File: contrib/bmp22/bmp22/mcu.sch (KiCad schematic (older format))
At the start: 42 parts, among them J301 USB_C_Receptacle_USB2.0, J302 Conn_ARM_JTAG_SWD_10, SW301 SW_DIP_x01, U301 USBLC6-2SC6, U302 STM32F103CBUx, Y301 8MHz

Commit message: added footprints
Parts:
- C301, C302, C303, C304, C305, C306, C309: footprint (none) -> Capacitor_SMD:C_0402_1005Metric
- C307, C308: footprint (none) -> Capacitor_SMD:C_0603_1608Metric
- D301, D302, D303, D304: footprint (none) -> LED_SMD:LED_0603_1608Metric
- J301: footprint (none) -> Connector_USB:USB_C_Receptacle_Palconn_UTC16-G
- J302: footprint (none) -> Connector:Tag-Connect_TC2050-IDC-NL_2x05_P1.27mm_Vertical
- R301, R302, R303, R304, R305, R308, R309, R310, R311, R312, R313, R314: footprint (none) -> Resistor_SMD:R_0402_1005Metric
- R306, R307: value R -> 5k1; footprint (none) -> Resistor_SMD:R_0402_1005Metric
- SW301: footprint (none) -> Button_Switch_SMD:SW_SPST_PTS810
- TP301, TP302, TP303, TP304, TP305, TP306, TP307, TP308, TP309: footprint (none) -> TestPoint:TestPoint_Pad_1.0x1.0mm

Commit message: created layout
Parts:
- TP301, TP302, TP303, TP304, TP305, TP306, TP307, TP309: footprint TestPoint:TestPoint_Pad_1.0x1.0mm -> TestPoint:TestPoint_Pad_D1.5mm
- TP308: value DIO -> SWDIO; footprint TestPoint:TestPoint_Pad_1.0x1.0mm -> TestPoint:TestPoint_Pad_D1.5mm
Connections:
- net +3V3: now also R311.1; no longer D301.2 (A)
- net GND: now also D301.1 (K), D302.1 (K), D303.1 (K), D304.1 (K); no longer R311.2, R312.2, R313.2, R314.2
- net LED0: now also R312.1; no longer D302.2 (A)
- net LED1: now also R313.1; no longer D303.2 (A)
- net LED2: now also R314.1; no longer D304.2 (A)
- net USBx1+: now also U301.6 (I/O1); no longer U301.4 (I/O2)
- net USBx1-: now also U301.4 (I/O2); no longer U301.6 (I/O1)
- net USBx2+: now also U301.1 (I/O1); no longer U301.3 (I/O2)
- net USBx2-: now also U301.3 (I/O2); no longer U301.1 (I/O1)
- net USB+ renamed USB_P
- net USB- renamed USB_N
- new net: D301.2 (A), R311.2
- new net: D302.2 (A), R312.2
- new net: D303.2 (A), R313.2
- new net: D304.2 (A), R314.2
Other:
- moved on the sheet: D301, D302, D303, D304, R311, R312, R313, R314, TP307, TP308, TP309
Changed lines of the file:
@@
 F 3 "https://www.st.com/resource/en/datasheet/usblc6-2.pdf" H 4150 3950 50  0001 C CNN
 	1    3950 3600
-	1    0    0    -1
+	-1   0    0    -1
 $EndComp
 $Comp
@@
 USBx2-
 Text Label 5550 3700 0    50   ~ 0
-USB-
+USB_N
 Text Label 5550 3500 0    50   ~ 0
-USB+
-Text Label 9300 5150 0    50   ~ 0
-USB+
-Text Label 9300 5050 0    50   ~ 0
-USB-
+USB_P
 Text Label 10150 4750 0    50   ~ 0
-USB+
+USB_P
 $Comp
 L Device:R R309
@@
 F 0 "TP301" H 7600 3150 50  0000 C CNN
 F 1 "~RST" H 7600 3050 50  0000 C CNN
-F 2 "TestPoint:TestPoint_Pad_1.0x1.0mm" H 7800 2850 50  0001 C CNN
+F 2 "TestPoint:TestPoint_Pad_D1.5mm" H 7800 2850 50  0001 C CNN
 F 3 "~" H 7800 2850 50  0001 C CNN
 	1    7600 2850
@@
 L Device:LED D301
 U 1 1 5F2F0E27
+P 1550 6700
+F 0 "D301" H 1550 6800 50  0000 C CNN
+F 1 "GREEN" H 1650 6600 50  0000 C CNN
+F 2 "LED_SMD:LED_0603_1608Metric" H 1550 6700 50  0001 C CNN
+F 3 "~" H 1550 6700 50  0001 C CNN
+	1    1550 6700
+	0    -1   -1   0
+$EndComp
+$Comp
+L Device:R R311
+U 1 1 5F2F3ADD
 P 1550 6400
-F 0 "D301" H 1550 6500 50  0000 C CNN
-F 1 "GREEN" H 1650 6300 50  0000 C CNN
-F 2 "LED_SMD:LED_0603_1608Metric" H 1550 6400 50  0001 C CNN
+F 0 "R311" V 1630 6400 50  0000 C CNN
+F 1 "330" V 1550 6400 50  0000 C CNN
+F 2 "Resistor_SMD:R_0402_1005Metric" V 1480 6400 50  0001 C CNN
 F 3 "~" H 1550 6400 50  0001 C CNN
 	1    1550 6400
-	0    -1   -1   0
-$EndComp
-$Comp
-L Device:R R311
-U 1 1 5F2F3ADD
-P 1550 6700
-F 0 "R311" V 1630 6700 50  0000 C CNN
-F 1 "330" V 1550 6700 50  0000 C CNN
-F 2 "Resistor_SMD:R_0402_1005Metric" V 1480 6700 50  0001 C CNN
-F 3 "~" H 1550 6700 50  0001 C CNN
-	1    1550 6700
 	1    0    0    -1
 $EndComp
@@
 L Device:LED D302
 U 1 1 5F2F57A5
+P 1850 6700
+F 0 "D302" H 1850 6800 50  0000 C CNN
+F 1 "RED" H 1900 6600 50  0000 C CNN
+F 2 "LED_SMD:LED_0603_1608Metric" H 1850 6700 50  0001 C CNN
+F 3 "~" H 1850 6700 50  0001 C CNN
+	1    1850 6700
+	0    -1   -1   0
+$EndComp
+$Comp
+L Device:R R312
+U 1 1 5F2F57AB
 P 1850 6400
-F 0 "D302" H 1850 6500 50  0000 C CNN
-F 1 "RED" H 1900 6300 50  0000 C CNN
-F 2 "LED_SMD:LED_0603_1608Metric" H 1850 6400 50  0001 C CNN
+F 0 "R312" V 1930 6400 50  0000 C CNN
+F 1 "330" V 1850 6400 50  0000 C CNN
+F 2 "Resistor_SMD:R_0402_1005Metric" V 1780 6400 50  0001 C CNN
 F 3 "~" H 1850 6400 50  0001 C CNN
 	1    1850 6400
-	0    -1   -1   0
-$EndComp
-$Comp
-L Device:R R312
-U 1 1 5F2F57AB
-P 1850 6700
-F 0 "R312" V 1930 6700 50  0000 C CNN
-F 1 "330" V 1850 6700 50  0000 C CNN
-F 2 "Resistor_SMD:R_0402_1005Metric" V 1780 6700 50  0001 C CNN
-F 3 "~" H 1850 6700 50  0001 C CNN
-	1    1850 6700
 	1    0    0    -1
 $EndComp
@@
 L Device:LED D303
 U 1 1 5F2F8AB8
+P 2150 6700
+F 0 "D303" H 2150 6800 50  0000 C CNN
+F 1 "ORANGE" H 2250 6600 50  0000 C CNN
+F 2 "LED_SMD:LED_0603_1608Metric" H 2150 6700 50  0001 C CNN
+F 3 "~" H 2150 6700 50  0001 C CNN
+	1    2150 6700
+	0    -1   -1   0
+$EndComp
+$Comp
+L Device:R R313
+U 1 1 5F2F8ABE
 P 2150 6400
-F 0 "D303" H 2150 6500 50  0000 C CNN
-F 1 "ORANGE" H 2250 6300 50  0000 C CNN
-F 2 "LED_SMD:LED_0603_1608Metric" H 2150 6400 50  0001 C CNN
+F 0 "R313" V 2230 6400 50  0000 C CNN
+F 1 "330" V 2150 6400 50  0000 C CNN
+F 2 "Resistor_SMD:R_0402_1005Metric" V 2080 6400 50  0001 C CNN
 F 3 "~" H 2150 6400 50  0001 C CNN
 	1    2150 6400
-	0    -1   -1   0
-$EndComp
-$Comp
-L Device:R R313
-U 1 1 5F2F8ABE
-P 2150 6700
-F 0 "R313" V 2230 6700 50  0000 C CNN
-F 1 "330" V 2150 6700 50  0000 C CNN
-F 2 "Resistor_SMD:R_0402_1005Metric" V 2080 6700 50  0001 C CNN
-F 3 "~" H 2150 6700 50  0001 C CNN
-	1    2150 6700
 	1    0    0    -1
 $EndComp
@@
 L Device:LED D304
 U 1 1 5F2F8ACA
+P 2450 6700
+F 0 "D304" H 2450 6800 50  0000 C CNN
+F 1 "YELLOW" H 2550 6600 50  0000 C CNN
+F 2 "LED_SMD:LED_0603_1608Metric" H 2450 6700 50  0001 C CNN
+F 3 "~" H 2450 6700 50  0001 C CNN
+	1    2450 6700
+	0    -1   -1   0
+$EndComp
+$Comp
+L Device:R R314
+U 1 1 5F2F8AD0
 P 2450 6400
-F 0 "D304" H 2450 6500 50  0000 C CNN
-F 1 "YELLOW" H 2550 6300 50  0000 C CNN
-F 2 "LED_SMD:LED_0603_1608Metric" H 2450 6400 50  0001 C CNN
+F 0 "R314" V 2530 6400 50  0000 C CNN
+F 1 "330" V 2450 6400 50  0000 C CNN
+F 2 "Resistor_SMD:R_0402_1005Metric" V 2380 6400 50  0001 C CNN
 F 3 "~" H 2450 6400 50  0001 C CNN
 	1    2450 6400
-	0    -1   -1   0
-$EndComp
-$Comp
-L Device:R R314
-U 1 1 5F2F8AD0
-P 2450 6700
-F 0 "R314" V 2530 6700 50  0000 C CNN
-F 1 "330" V 2450 6700 50  0000 C CNN
-F 2 "Resistor_SMD:R_0402_1005Metric" V 2380 6700 50  0001 C CNN
-F 3 "~" H 2450 6700 50  0001 C CNN
-	1    2450 6700
 	1    0    0    -1
 $EndComp
@@
 L power:GND #PWR0342
 U 1 1 5F39D67B
-P 3800 7150
-F 0 "#PWR0342" H 3800 6900 50  0001 C CNN
-F 1 "GND" H 3800 7000 50  0000 C CNN
-F 2 "" H 3800 7150 50  0001 C CNN
-F 3 "" H 3800 7150 50  0001 C CNN
-	1    3800 7150
-	1    0    0    -1
-$EndComp
-Wire Wire Line
-	3800 7150 3800 7100
-Text Label 3400 7100 3    50   ~ 0
+P 4050 7150
+F 0 "#PWR0342" H 4050 6900 50  0001 C CNN
+F 1 "GND" H 4050 7000 50  0000 C CNN
+F 2 "" H 4050 7150 50  0001 C CNN
+F 3 "" H 4050 7150 50  0001 C CNN
+	1    4050 7150
+	1    0    0    -1
+$EndComp
+Wire Wire Line
+	4050 7150 4050 7100
+Text Label 3450 7100 3    50   ~ 0
 SWDCLK
 $Comp
 L Connector:TestPoint TP309
 U 1 1 5F3A190C
-P 3800 7100
-F 0 "TP309" H 3800 7370 50  0000 C CNN
-F 1 "GND" H 3800 7300 50  0000 C CNN
-F 2 "TestPoint:TestPoint_Pad_1.0x1.0mm" H 4000 7100 50  0001 C CNN
-F 3 "~" H 4000 7100 50  0001 C CNN
-	1    3800 7100
-	1    0    0    -1
-$EndComp
-Text Label 3600 7100 3    50   ~ 0
+P 4050 7100
+F 0 "TP309" H 4050 7370 50  0000 C CNN
+F 1 "GND" H 4050 7300 50  0000 C CNN
+F 2 "TestPoint:TestPoint_Pad_D1.5mm" H 4250 7100 50  0001 C CNN
+F 3 "~" H 4250 7100 50  0001 C CNN
+	1    4050 7100
+	1    0    0    -1
+$EndComp
+Text Label 3750 7100 3    50   ~ 0
 SDWIO
-$Comp
-L Connector:TestPoint TP308
-U 1 1 5F3A950D
-P 3600 7100
-F 0 "TP308" H 3600 7370 50  0000 C CNN
-F 1 "DIO" H 3600 7300 50  0000 C CNN
-F 2 "TestPoint:TestPoint_Pad_1.0x1.0mm" H 3800 7100 50  0001 C CNN
-F 3 "~" H 3800 7100 50  0001 C CNN
-	1    3600 7100
-	1    0    0    -1
-$EndComp
 $Comp
 L Connector:TestPoint TP307
 U 1 1 5F3A9E23
-P 3400 7100
-F 0 "TP307" H 3400 7370 50  0000 C CNN
-F 1 "CLK" H 3400 7300 50  0000 C CNN
-F 2 "TestPoint:TestPoint_Pad_1.0x1.0mm" H 3600 7100 50  0001 C CNN
-F 3 "~" H 3600 7100 50  0001 C CNN
-	1    3400 7100
+P 3450 7100
+F 0 "TP307" H 3450 7370 50  0000 C CNN
+F 1 "CLK" H 3450 7300 50  0000 C CNN
+F 2 "TestPoint:TestPoint_Pad_D1.5mm" H 3650 7100 50  0001 C CNN
+F 3 "~" H 3650 7100 50  0001 C CNN
+	1    3450 7100
 	1    0    0    -1
 $EndComp
@@
 F 0 "TP306" H 3150 7370 50  0000 C CNN
 F 1 "SWO" H 3150 7300 50  0000 C CNN
-F 2 "TestPoint:TestPoint_Pad_1.0x1.0mm" H 3350 7100 50  0001 C CNN
+F 2 "TestPoint:TestPoint_Pad_D1.5mm" H 3350 7100 50  0001 C CNN
 F 3 "~" H 3350 7100 50  0001 C CNN
 	1    3150 7100
@@
 F 0 "TP302" H 2400 3270 50  0000 C CNN
 F 1 "+5V" H 2400 3200 50  0000 C CNN
-F 2 "TestPoint:TestPoint_Pad_1.0x1.0mm" H 2600 3000 50  0001 C CNN
+F 2 "TestPoint:TestPoint_Pad_D1.5mm" H 2600 3000 50  0001 C CNN
 F 3 "~" H 2600 3000 50  0001 C CNN
 	1    2400 3000
@@
 F 0 "TP304" H 4650 3670 50  0000 C CNN
 F 1 "USBx1+" H 4650 3600 50  0000 C CNN
-F 2 "TestPoint:TestPoint_Pad_1.0x1.0mm" H 4850 3400 50  0001 C CNN
+F 2 "TestPoint:TestPoint_Pad_D1.5mm" H 4850 3400 50  0001 C CNN
 F 3 "~" H 4850 3400 50  0001 C CNN
 	1    4650 3400
@@
 F 0 "TP305" H 2050 4670 50  0000 C CNN
 F 1 "GND" H 2050 4600 50  0000 C CNN
-F 2 "TestPoint:TestPoint_Pad_1.0x1.0mm" H 2250 4400 50  0001 C CNN
+F 2 "TestPoint:TestPoint_Pad_D1.5mm" H 2250 4400 50  0001 C CNN
 F 3 "~" H 2250 4400 50  0001 C CNN
 	1    2050 4400
@@
 F 0 "TP303" H 3250 3670 50  0000 C CNN
 F 1 "USBx1-" H 3250 3600 50  0000 C CNN
-F 2 "TestPoint:TestPoint_Pad_1.0x1.0mm" H 3450 3400 50  0001 C CNN
+F 2 "TestPoint:TestPoint_Pad_D1.5mm" H 3450 3400 50  0001 C CNN
 F 3 "~" H 3450 3400 50  0001 C CNN
 	1    3250 3400
@@
 	1    0    0    -1
 $EndComp
+Text Label 9300 5050 0    50   ~ 0
+USB_N
+Text Label 9300 5150 0    50   ~ 0
+USB_P
+$Comp
+L Connector:TestPoint TP308
+U 1 1 5F3A950D
+P 3750 7100
+F 0 "TP308" H 3750 7370 50  0000 C CNN
+F 1 "SWDIO" H 3750 7300 50  0000 C CNN
+F 2 "TestPoint:TestPoint_Pad_D1.5mm" H 3950 7100 50  0001 C CNN
+F 3 "~" H 3950 7100 50  0001 C CNN
+	1    3750 7100
+	1    0    0    -1
+$EndComp

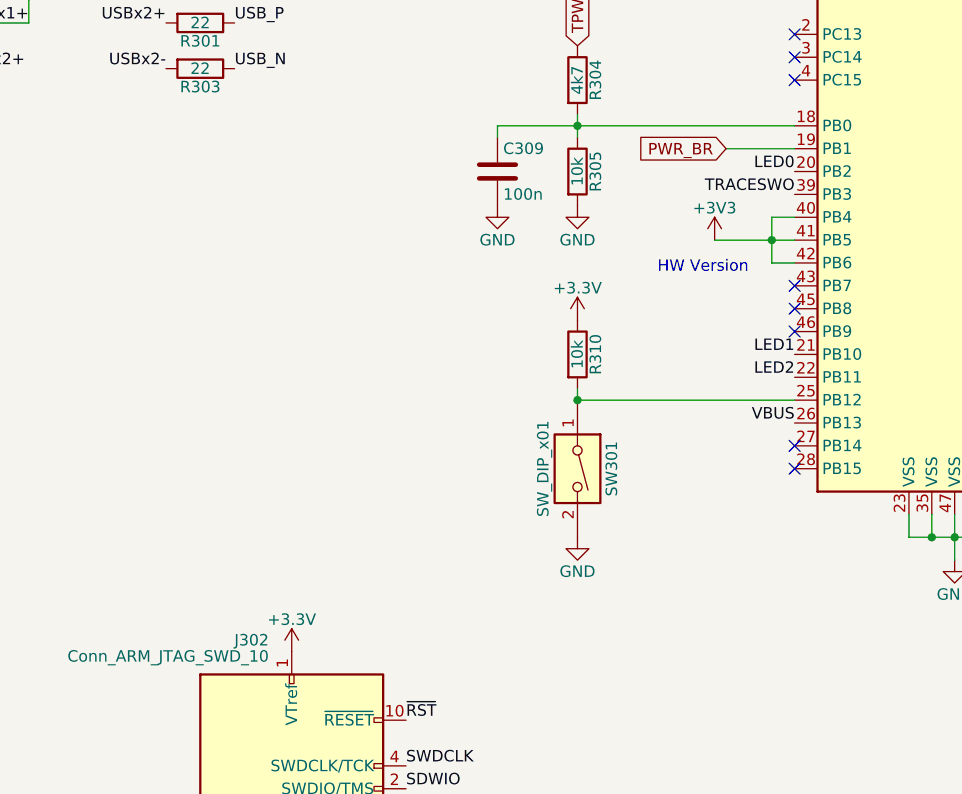
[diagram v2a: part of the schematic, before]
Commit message: added hardware identification option and TDO optional UART connection
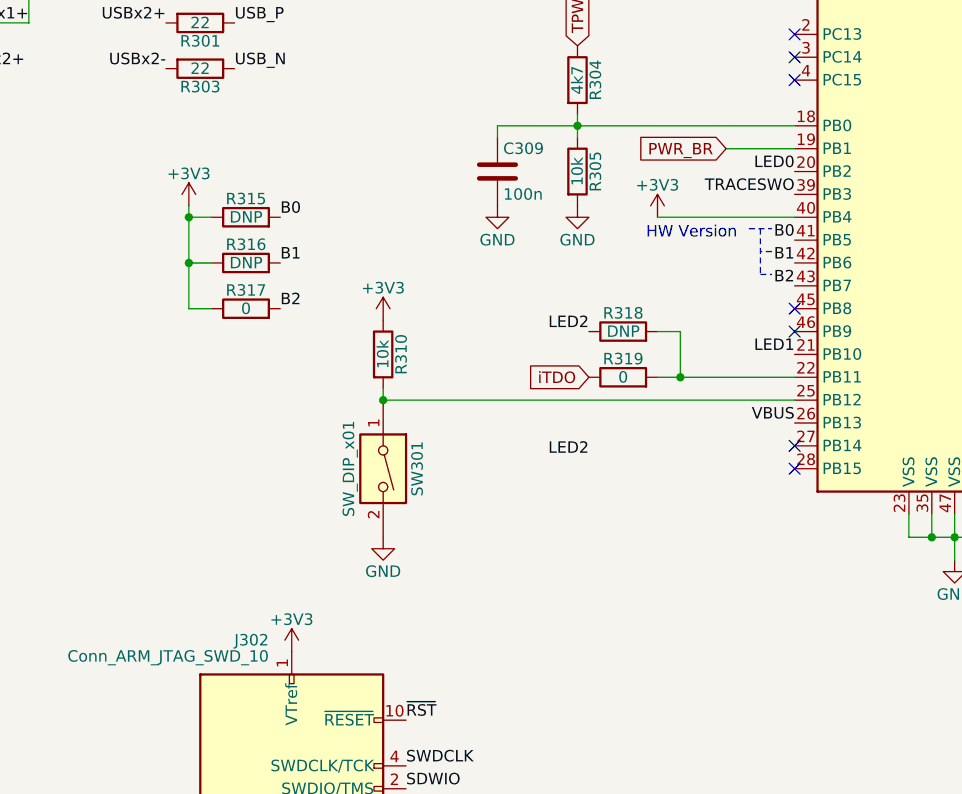
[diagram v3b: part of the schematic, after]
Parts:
- added R315, R316, R318: DNP, Resistor_SMD:R_0402_1005Metric, symbol Device:R
- added R317, R319: 0, Resistor_SMD:R_0402_1005Metric, symbol Device:R
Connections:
- net +3V3: now also R315.1, R316.1, R317.1; no longer U302.41 (PB5), U302.42 (PB6)
- net LED2: now also R318.1; no longer U302.22 (PB11)
- net iTDO: now also R319.1
- net B2: now reaches U302.43 (PB7)
- net B2: now also R317.2
- new net: R318.2, R319.2, U302.22 (PB11)
- new net B0: R315.2, U302.41 (PB5)
- new net B1: R316.2, U302.42 (PB6)
- no-connect marks 13 -> 12
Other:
- moved on the sheet: R310, SW301
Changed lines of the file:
@@
 L Switch:SW_DIP_x01 SW301
 U 1 1 5F254BC9
-P 7050 5450
-F 0 "SW301" H 7050 5600 50  0000 C CNN
-F 1 "SW_DIP_x01" H 7050 5300 50  0000 C CNN
-F 2 "Button_Switch_SMD:SW_SPST_PTS810" H 7050 5450 50  0001 C CNN
-F 3 "~" H 7050 5450 50  0001 C CNN
-	1    7050 5450
+P 6200 5450
+F 0 "SW301" H 6200 5600 50  0000 C CNN
+F 1 "SW_DIP_x01" H 6200 5300 50  0000 C CNN
+F 2 "Button_Switch_SMD:SW_SPST_PTS810" H 6200 5450 50  0001 C CNN
+F 3 "~" H 6200 5450 50  0001 C CNN
+	1    6200 5450
 	0    1    1    0
 $EndComp
@@
 Text Label 8000 4150 2    50   ~ 0
 LED0
-Text Notes 7400 4600 0    50   ~ 0
+Text Notes 7350 4450 0    50   ~ 0
 HW Version
-NoConn ~ 8000 4650
-Wire Wire Line
-	8000 4550 7900 4550
-Wire Wire Line
-	7900 4550 7900 4450
-Wire Wire Line
-	7900 4450 8000 4450
-Wire Wire Line
-	8000 4350 7900 4350
-Wire Wire Line
-	7900 4350 7900 4450
-Connection ~ 7900 4450
-Wire Wire Line
-	7650 4450 7900 4450
 NoConn ~ 8000 4750
 NoConn ~ 8000 4850
 Text Label 8000 4950 2    50   ~ 0
 LED1
-Text Label 8000 5050 2    50   ~ 0
+Text Label 7100 4850 2    50   ~ 0
 LED2
 $Comp
 L Device:R R310
 U 1 1 5F2E1EF5
-P 7050 4950
-F 0 "R310" V 7130 4950 50  0000 C CNN
-F 1 "10k" V 7050 4950 50  0000 C CNN
-F 2 "Resistor_SMD:R_0402_1005Metric" V 6980 4950 50  0001 C CNN
-F 3 "~" H 7050 4950 50  0001 C CNN
-	1    7050 4950
-	1    0    0    -1
-$EndComp
-$Comp
-L power:+3.3V #PWR0332
-U 1 1 5F2E2317
-P 7050 4800
-F 0 "#PWR0332" H 7050 4650 50  0001 C CNN
-F 1 "+3.3V" H 7050 4940 50  0000 C CNN
-F 2 "" H 7050 4800 50  0001 C CNN
-F 3 "" H 7050 4800 50  0001 C CNN
-	1    7050 4800
-	1    0    0    -1
-$EndComp
-Wire Wire Line
-	8000 5150 7050 5150
-Wire Wire Line
-	7050 5150 7050 5100
-Connection ~ 7050 5150
+P 6200 4950
+F 0 "R310" V 6280 4950 50  0000 C CNN
+F 1 "10k" V 6200 4950 50  0000 C CNN
+F 2 "Resistor_SMD:R_0402_1005Metric" V 6130 4950 50  0001 C CNN
+F 3 "~" H 6200 4950 50  0001 C CNN
+	1    6200 4950
+	1    0    0    -1
+$EndComp
+Wire Wire Line
+	8000 5150 6200 5150
+Wire Wire Line
+	6200 5150 6200 5100
+Connection ~ 6200 5150
 $Comp
 L power:GND #PWR0334
 U 1 1 5F2EAA2C
-P 7050 5750
-F 0 "#PWR0334" H 7050 5500 50  0001 C CNN
-F 1 "GND" H 7050 5600 50  0000 C CNN
-F 2 "" H 7050 5750 50  0001 C CNN
-F 3 "" H 7050 5750 50  0001 C CNN
-	1    7050 5750
+P 6200 5750
+F 0 "#PWR0334" H 6200 5500 50  0001 C CNN
+F 1 "GND" H 6200 5600 50  0000 C CNN
+F 2 "" H 6200 5750 50  0001 C CNN
+F 3 "" H 6200 5750 50  0001 C CNN
+	1    6200 5750
 	1    0    0    -1
 $EndComp
@@
 L power:+3V3 #PWR0329
 U 1 1 5F315565
-P 7650 4450
-F 0 "#PWR0329" H 7650 4300 50  0001 C CNN
-F 1 "+3V3" H 7650 4590 50  0000 C CNN
-F 2 "" H 7650 4450 50  0001 C CNN
-F 3 "" H 7650 4450 50  0001 C CNN
-	1    7650 4450
+P 7400 4350
+F 0 "#PWR0329" H 7400 4200 50  0001 C CNN
+F 1 "+3V3" H 7400 4490 50  0000 C CNN
+F 2 "" H 7400 4350 50  0001 C CNN
+F 3 "" H 7400 4350 50  0001 C CNN
+	1    7400 4350
 	1    0    0    -1
 $EndComp
@@
 ~RST
 $Comp
-L power:+3.3V #PWR0337
-U 1 1 5F39A841
-P 5800 6250
-F 0 "#PWR0337" H 5800 6100 50  0001 C CNN
-F 1 "+3.3V" H 5800 6390 50  0000 C CNN
-F 2 "" H 5800 6250 50  0001 C CNN
-F 3 "" H 5800 6250 50  0001 C CNN
-	1    5800 6250
-	1    0    0    -1
-$EndComp
-$Comp
 L power:GND #PWR0342
 U 1 1 5F39D67B
@@
 	1    0    0    -1
 $EndComp
+Text GLabel 7100 5050 0    50   Input ~ 0
+iTDO
+$Comp
+L Device:R R319
+U 1 1 5F1694D2
+P 7250 5050
+F 0 "R319" V 7330 5050 50  0000 C CNN
+F 1 "0" V 7250 5050 50  0000 C CNN
+F 2 "Resistor_SMD:R_0402_1005Metric" V 7180 5050 50  0001 C CNN
+F 3 "~" H 7250 5050 50  0001 C CNN
+	1    7250 5050
+	0    -1   -1   0
+$EndComp
+Wire Wire Line
+	7400 5050 7500 5050
+$Comp
+L Device:R R318
+U 1 1 5F16E85C
+P 7250 4850
+F 0 "R318" V 7330 4850 50  0000 C CNN
+F 1 "DNP" V 7250 4850 50  0000 C CNN
+F 2 "Resistor_SMD:R_0402_1005Metric" V 7180 4850 50  0001 C CNN
+F 3 "~" H 7250 4850 50  0001 C CNN
+	1    7250 4850
+	0    -1   -1   0
+$EndComp
+Wire Wire Line
+	7400 4850 7500 4850
+Wire Wire Line
+	7500 4850 7500 5050
+Connection ~ 7500 5050
+Wire Wire Line
+	7500 5050 8000 5050
+Text Label 7100 5400 2    50   ~ 0
+LED2
+$Comp
+L Device:R R317
+U 1 1 5F17213D
+P 5600 4750
+F 0 "R317" V 5680 4750 50  0000 C CNN
+F 1 "0" V 5600 4750 50  0000 C CNN
+F 2 "Resistor_SMD:R_0402_1005Metric" V 5530 4750 50  0001 C CNN
+F 3 "~" H 5600 4750 50  0001 C CNN
+	1    5600 4750
+	0    -1   -1   0
+$EndComp
+$Comp
+L Device:R R316
+U 1 1 5F1733D8
+P 5600 4550
+F 0 "R316" V 5680 4550 50  0000 C CNN
+F 1 "DNP" V 5600 4550 50  0000 C CNN
+F 2 "Resistor_SMD:R_0402_1005Metric" V 5530 4550 50  0001 C CNN
+F 3 "~" H 5600 4550 50  0001 C CNN
+	1    5600 4550
+	0    -1   -1   0
+$EndComp
+$Comp
+L Device:R R315
+U 1 1 5F175D2C
+P 5600 4350
+F 0 "R315" V 5680 4350 50  0000 C CNN
+F 1 "DNP" V 5600 4350 50  0000 C CNN
+F 2 "Resistor_SMD:R_0402_1005Metric" V 5530 4350 50  0001 C CNN
+F 3 "~" H 5600 4350 50  0001 C CNN
+	1    5600 4350
+	0    -1   -1   0
+$EndComp
+$Comp
+L power:+3V3 #PWR0344
+U 1 1 5F177B83
+P 5800 6250
+F 0 "#PWR0344" H 5800 6100 50  0001 C CNN
+F 1 "+3V3" H 5800 6390 50  0000 C CNN
+F 2 "" H 5800 6250 50  0001 C CNN
+F 3 "" H 5800 6250 50  0001 C CNN
+	1    5800 6250
+	1    0    0    -1
+$EndComp
+$Comp
+L power:+3V3 #PWR0337
+U 1 1 5F178281
+P 6200 4800
+F 0 "#PWR0337" H 6200 4650 50  0001 C CNN
+F 1 "+3V3" H 6200 4940 50  0000 C CNN
+F 2 "" H 6200 4800 50  0001 C CNN
+F 3 "" H 6200 4800 50  0001 C CNN
+	1    6200 4800
+	1    0    0    -1
+$EndComp
+Wire Wire Line
+	7400 4350 8000 4350
+Text Label 8000 4450 2    50   ~ 0
+B0
+Text Label 8000 4550 2    50   ~ 0
+B1
+Text Label 8000 4650 2    50   ~ 0
+B2
+Wire Notes Line
+	7850 4400 7850 4600
+Wire Notes Line
+	7850 4600 7900 4600
+Wire Notes Line
+	7900 4500 7850 4500
+Wire Notes Line
+	7800 4400 7900 4400
+Text Label 5750 4350 0    50   ~ 0
+B0
+Text Label 5750 4550 0    50   ~ 0
+B1
+Text Label 5750 4750 0    50   ~ 0
+B2
+$Comp
+L power:+3V3 #PWR0332
+U 1 1 5F192667
+P 5350 4300
+F 0 "#PWR0332" H 5350 4150 50  0001 C CNN
+F 1 "+3V3" H 5350 4440 50  0000 C CNN
+F 2 "" H 5350 4300 50  0001 C CNN
+F 3 "" H 5350 4300 50  0001 C CNN
+	1    5350 4300
+	1    0    0    -1
+$EndComp
+Wire Wire Line
+	5350 4300 5350 4350
+Wire Wire Line
+	5350 4750 5450 4750
+Wire Wire Line
+	5450 4550 5350 4550
+Connection ~ 5350 4550
+Wire Wire Line
+	5350 4550 5350 4750
+Wire Wire Line
+	5450 4350 5350 4350
+Connection ~ 5350 4350
+Wire Wire Line
+	5350 4350 5350 4550
 $EndSCHEMATC
